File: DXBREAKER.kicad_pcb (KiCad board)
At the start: 2 copper layers, 25.4 x 38.1 mm, 19 parts, among them J1 PINS_LEFT, J2 PINS_RIGHT, SW1 RESET, SW2 FLASH, U1 ESP-12F

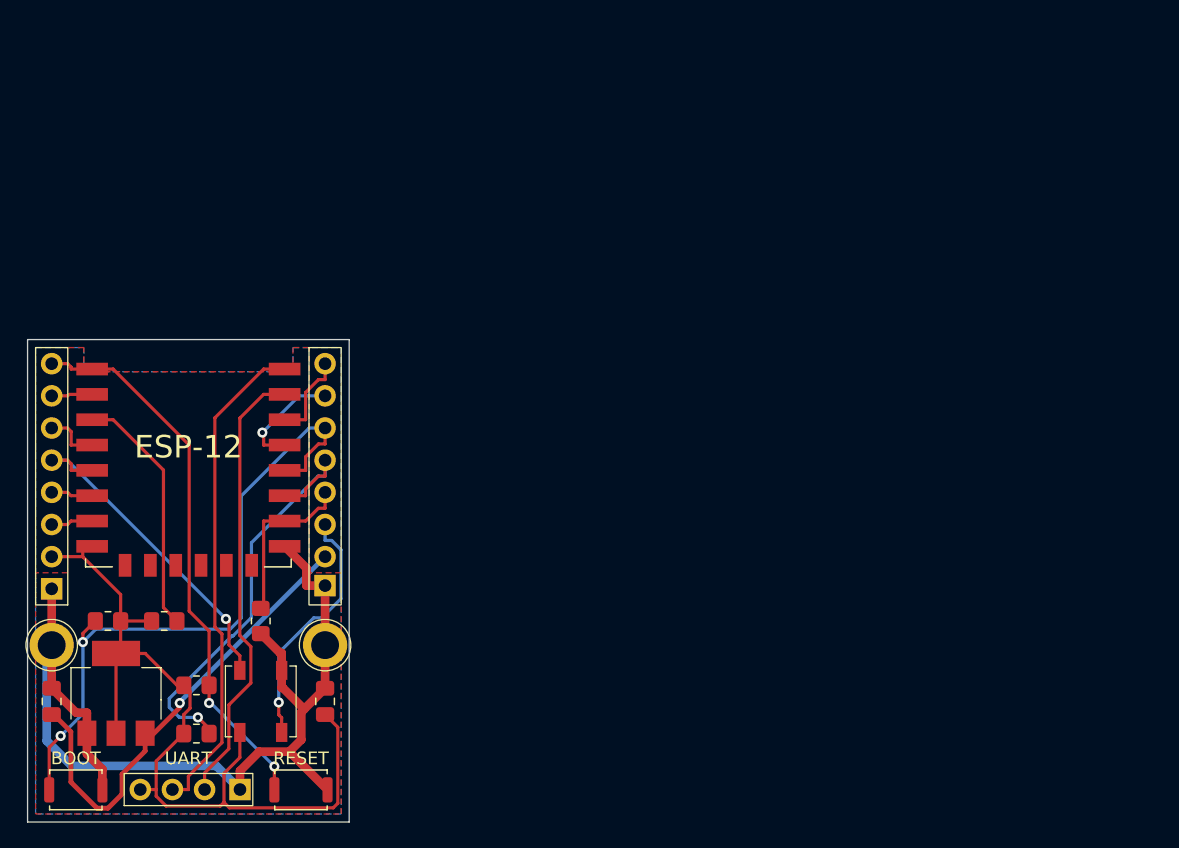
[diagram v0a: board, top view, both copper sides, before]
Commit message: Update schematics for Rev.2.0
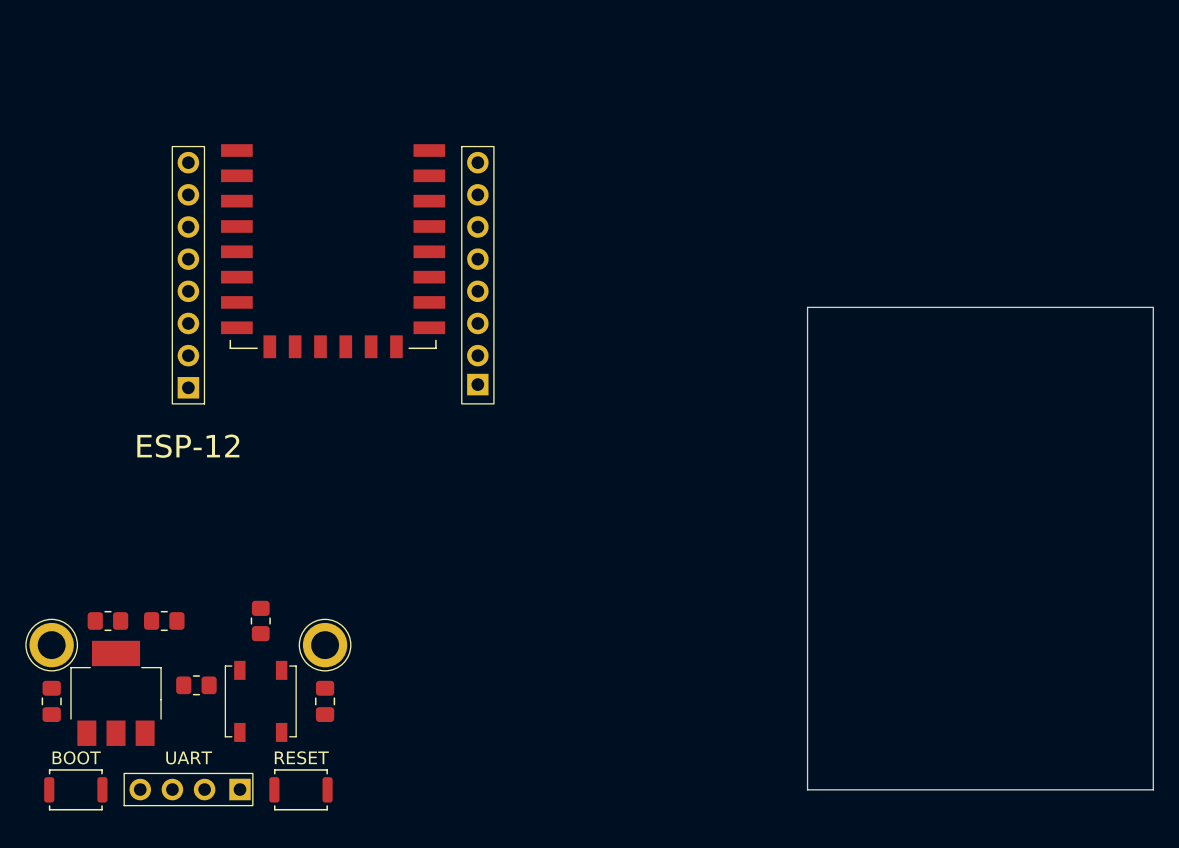
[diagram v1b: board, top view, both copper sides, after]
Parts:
- removed the G*** at (126.4, 99.1)
- removed R3: 10k, Resistor_SMD:R_0805_2012Metric_Pad1.20x1.40mm_HandSolder
- moved U1 20.7 mm to (138.4, 78.7)
- moved J2 19.9 mm to (149.9, 76.2)
- moved J1 19.2 mm to (127.0, 94.0)
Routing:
- net Earth: track 80.0 -> 0.00 mm
- net VCC: track 68.2 -> 0.00 mm
- net /GPIO0: track 52.6 -> 0.00 mm, vias 2 -> 0
- net /RESET: track 43.7 -> 0.00 mm, vias 2 -> 0
- net Net-(Jr1-Pin_2): track 39.0 -> 0.00 mm
- net /VIN: track 37.5 -> 0.00 mm, vias 1 -> 0
- net Net-(Jr1-Pin_3): track 35.5 -> 0.00 mm
- net /GPIO2: track 34.6 -> 0.00 mm, vias 1 -> 0
- net /GPIO14: track 27.3 -> 0.00 mm, vias 1 -> 0
- net /DOUT: track 19.8 -> 0.00 mm, vias 1 -> 0
- net Net-(U1-EN): track 19.6 -> 0.00 mm
- net /GPIO15: track 13.5 -> 0.00 mm
- net /GPIO4: track 8.84 -> 0.00 mm, vias 1 -> 0
- net /GPIO5: track 7.03 -> 0.00 mm
- net /GPIO16: track 4.38 -> 0.00 mm
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- removed copper zone on B.Cu, net Earth
- removed copper zone on F.Cu, net Earth
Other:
- board size 25.4 x 38.1 mm -> 27.3 x 38.1 mm

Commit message: oopsie
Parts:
- added D2: WS2812B, LED_SMD:LED_WS2812B_PLCC4_5.0x5.0mm_P3.2mm, F.Cu at (147.4, 100.7)
- added D3: WS2812B, LED_SMD:LED_WS2812B_PLCC4_5.0x5.0mm_P3.2mm, F.Cu at (147.4, 107.3)
- added D4: WS2812B, LED_SMD:LED_WS2812B_PLCC4_5.0x5.0mm_P3.2mm, F.Cu at (147.4, 113.9)
- renumbered D1 to D1-4, Ue to U2
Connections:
- D1-4 pad 2: /DOUT -> Net-(D1-4-DOUT)

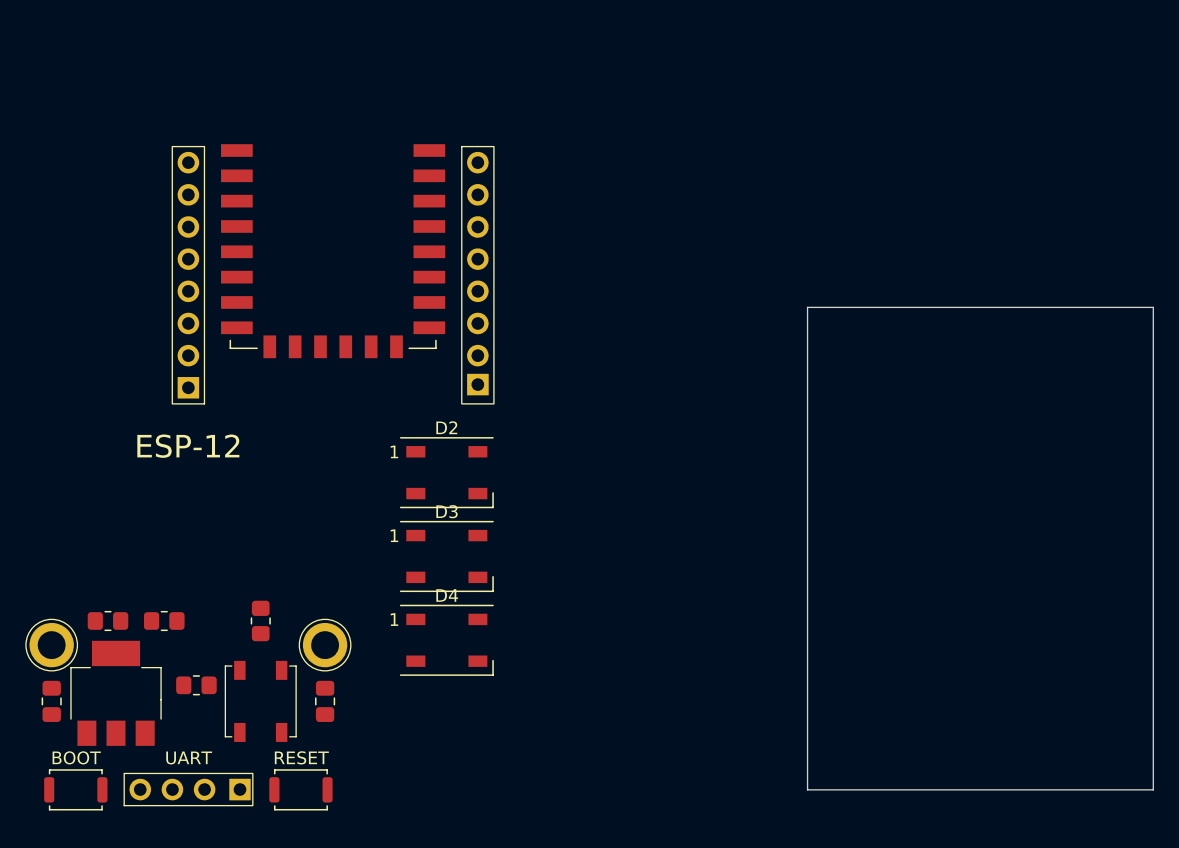
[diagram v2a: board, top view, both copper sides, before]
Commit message: new board layout, added neopixel matrix
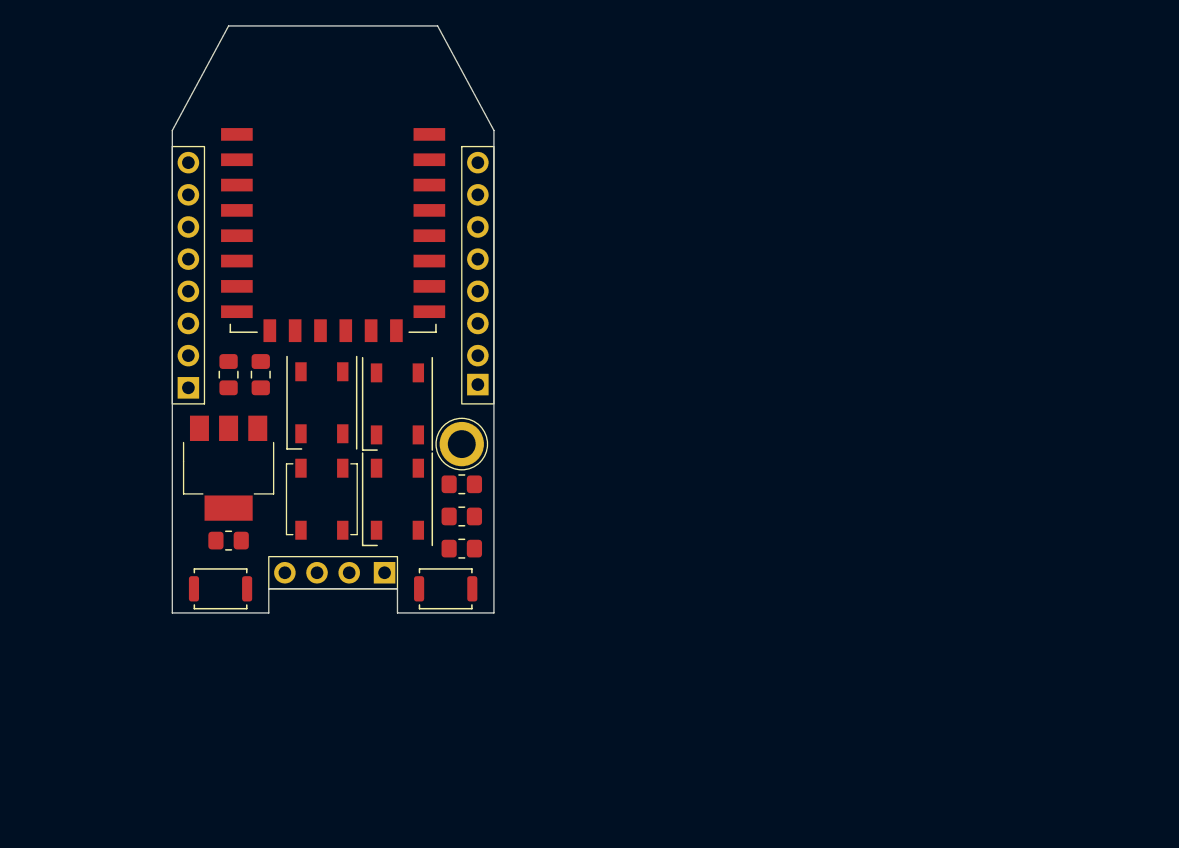
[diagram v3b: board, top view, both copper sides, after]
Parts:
- removed G***: LOGO, LOGO
- removed hole2: MountingHole_2.2mm_M2_ISO7380_Pad, MountingHole:MountingHole_2.2mm_M2_ISO7380_Pad
- moved C1 29.3 mm to (130.2, 92.9)
- moved R4 28.5 mm to (148.6, 106.7)
- moved C2 26.3 mm to (132.7, 92.9)
- moved R5 25.9 mm to (148.6, 101.6), turned to 180 degrees
- moved R1 24.8 mm to (148.6, 104.1), turned to 180 degrees
- moved Jr1 20.6 mm to (134.6, 108.6)
- moved U2 19.9 mm to (130.2, 100.3), turned to -90 degrees
- moved SW1 19.6 mm to (147.3, 109.9)
- moved SW2 19.6 mm to (129.5, 109.9)
- moved DX 19.2 mm to (148.6, 98.4)
- moved D4 19.1 mm to (143.5, 95.2), turned to -90 degrees
- moved D1-4 16.7 mm to (137.5, 102.8), turned to -90 degrees
- moved D2 11.3 mm to (137.5, 95.2), turned to -90 degrees
- moved R2 6.84 mm to (130.2, 106.0), turned to 180 degrees
- moved D3 5.97 mm to (143.5, 102.8), turned to -90 degrees
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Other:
- board size 27.3 x 38.1 mm -> 25.4 x 46.4 mm
- board text removed: "BOOT"
- board text removed: "DX8266 Dev Board"
- board text removed: "Designed in Chile"
- board text removed: "ESP-12"
- board text removed: "RESET"
- board text removed: "UART"
